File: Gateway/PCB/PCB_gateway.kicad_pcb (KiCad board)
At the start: 2 copper layers, 38 x 52 mm, 39 parts, among them J1 USB4215-03-A_REVA, J2 Conn_01x06_Pin, J3 Conn_01x04_Pin, J4 Conn_01x04_Pin, U1 ESP32-C3-WROOM-02U-N4, U2 BME680, U4 AMS1117-3.3

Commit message: Add files via upload
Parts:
- added R12: 0, Resistor_SMD:R_0805_2012Metric_Pad1.20x1.40mm_HandSolder, F.Cu at (185.1, 109.8)
- added R13: 0, Resistor_SMD:R_0805_2012Metric_Pad1.20x1.40mm_HandSolder, F.Cu at (185.1, 112.1)
- D3: value D_Schottky_Small_Filled -> D_Schottky
- moved R9 2.81 mm to (185.1, 107.4), turned to 180 degrees
- moved U4 0.62 mm to (177.1, 111.6)
- renumbered S2 to BOOT, S1 to EN1, D1 to LED, D2 to POWER
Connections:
- J1 pad A6: D+ -> Net-(J1-DP1)
- J1 pad A7: D- -> Net-(J1-DN1)
- J1 pad B6: D+ -> Net-(J1-DP1)
- J1 pad B7: D- -> Net-(J1-DN1)
- J3 pad 2: RX -> TX
- J3 pad 3: TX -> RX
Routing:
- net Net-(J1-DP1): track 0.00 -> 32.4 mm
- net GPIO3: track 27.9 -> 52.8 mm
- net Net-(J1-DN1): track 0.00 -> 18.3 mm
- net D+: track 41.7 -> 23.9 mm
- net D-: track 38.9 -> 21.2 mm
- net +3.3V: track 156.2 -> 142.0 mm, vias 0 -> 2
- net LED: track 29.3 -> 40.7 mm
- net GND: track 27.0 -> 16.5 mm, vias 26 -> 57
- net SDA: track 33.0 -> 42.5 mm, vias 2 -> 5
- net BOOT: track 41.9 -> 35.4 mm
- net EN: track 60.6 -> 67.1 mm
- net TX: track 8.93 -> 4.40 mm
- net GPIO4: track 27.9 -> 24.2 mm
- net Net-(D3-A): track 9.09 -> 11.4 mm, vias 0 -> 2
- net SCL: track 28.6 -> 30.7 mm
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
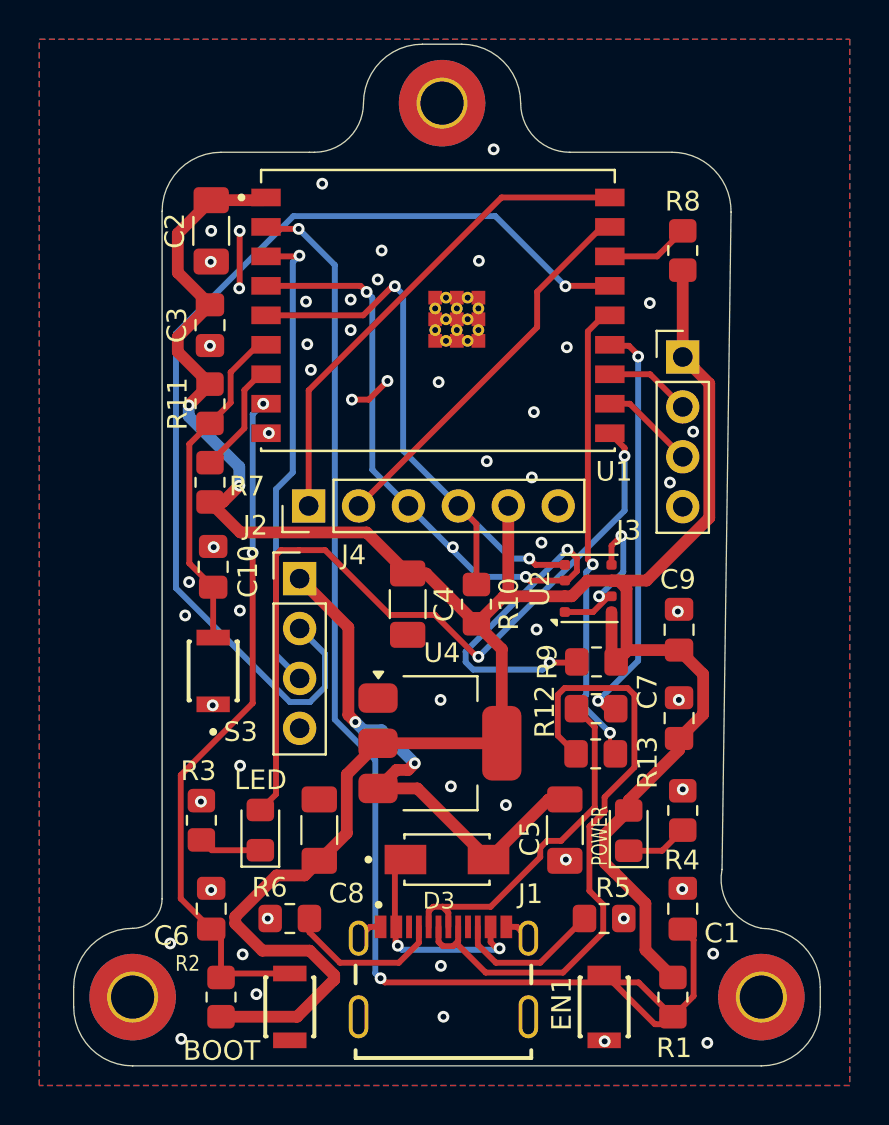
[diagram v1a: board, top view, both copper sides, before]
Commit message: Update PCB design
DRC errors opgelost, teardrops toegevoegd, routing optimaliseren, kleine details
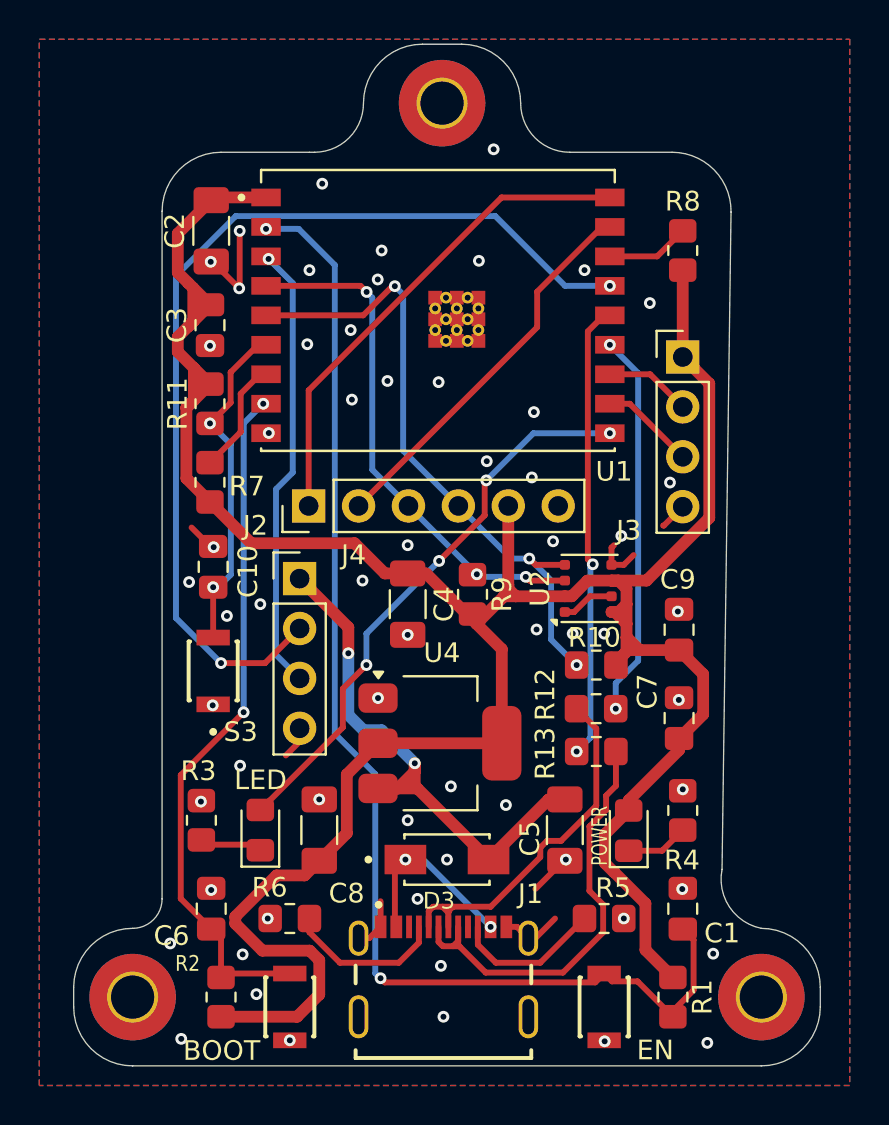
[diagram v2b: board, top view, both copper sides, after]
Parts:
- moved R9 7.19 mm to (178.8, 104.0), turned to 90 degrees
- moved R10 6.84 mm to (185.1, 107.6), turned to 0 degrees
- moved R13 0.12 mm to (185.1, 112.0), turned to 0 degrees
- renumbered EN1 to EN
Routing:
- net SDA: track 42.5 -> 26.6 mm, vias 5 -> 3
- net LED: track 40.7 -> 29.5 mm, vias 2 -> 4
- net Net-(J1-DP1): track 32.4 -> 23.2 mm
- net GND: track 16.5 -> 21.9 mm, vias 57 -> 62
- net EN: track 67.1 -> 63.4 mm
- net +3.3V: track 142.0 -> 145.4 mm, vias 2 -> 0
- net GPIO3: track 52.8 -> 50.2 mm, vias 1 -> 2
- net SCL: track 30.7 -> 32.8 mm, vias 2 -> 3
- net Net-(D3-A): track 11.4 -> 9.43 mm
- net +5V: track 27.0 -> 28.6 mm
- net GPIO4: track 24.2 -> 22.9 mm
- net D-: track 21.2 -> 20.2 mm
- net D+: track 23.9 -> 23.3 mm
- net GPIO7: vias 0 -> 2

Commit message: update silkscreen
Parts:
- removed the G*** at (177.4, 105.5)
- added G***: LOGO, LOGO, B.Cu at (177.4, 99.4)
- added G***: LOGO, LOGO, B.Cu at (176.3, 110.2)
- moved G*** 4.20 mm to (183.0, 107.7)
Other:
- board text added: "if my grandmother had wheels, she would have been a bike"

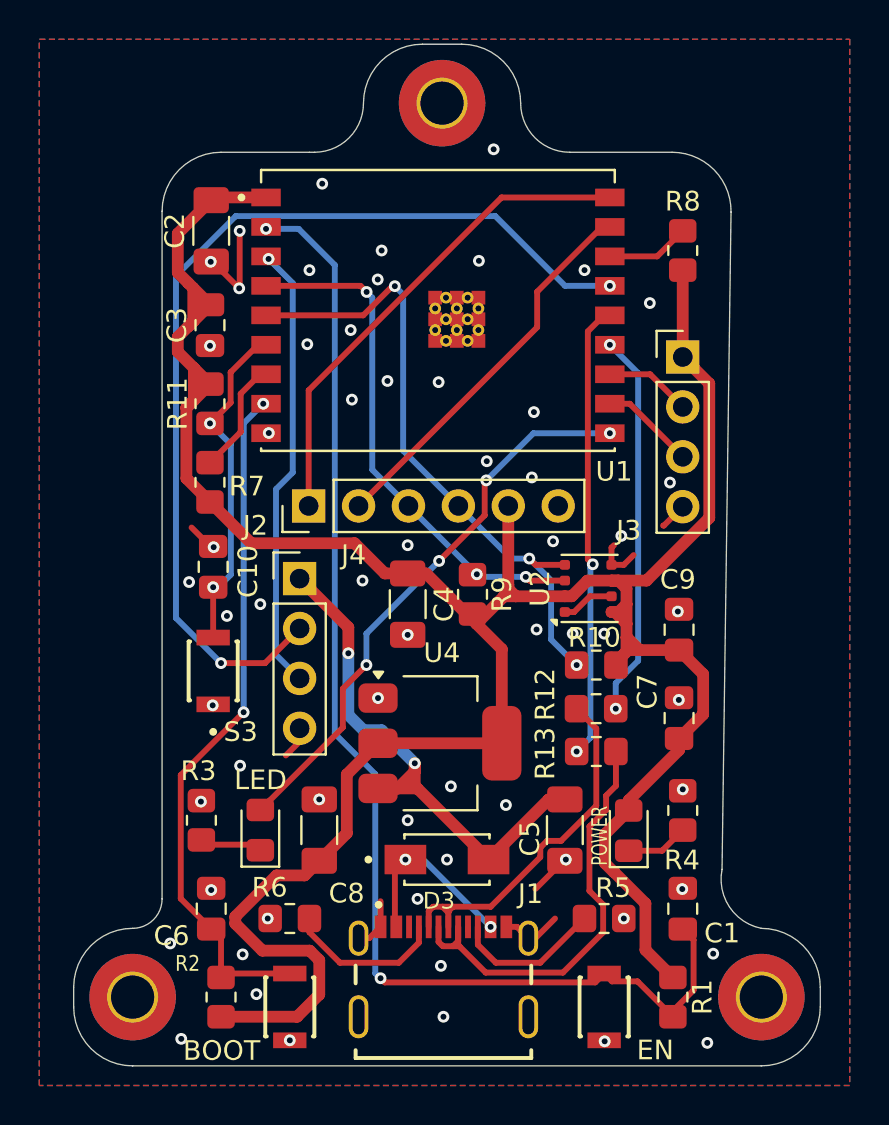
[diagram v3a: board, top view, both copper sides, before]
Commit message: Header silkscreen
added pin description for each header on the silkscreen
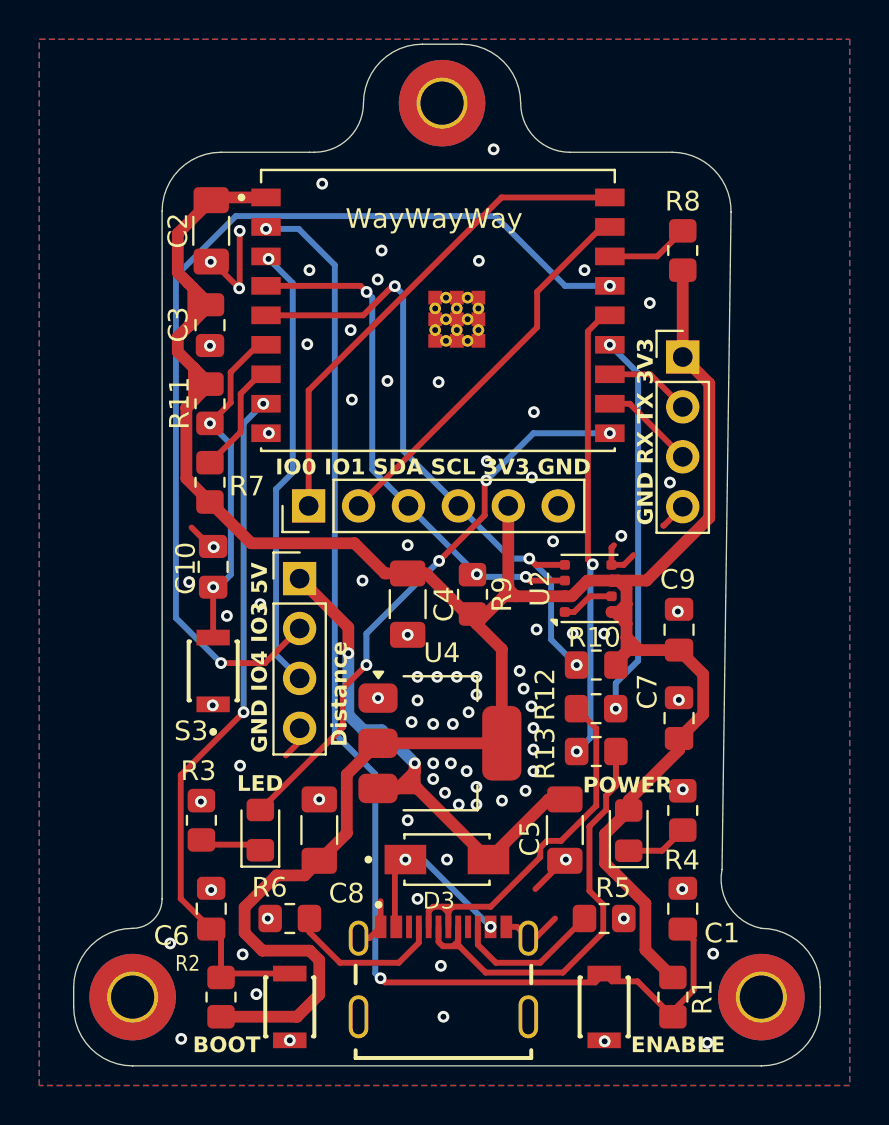
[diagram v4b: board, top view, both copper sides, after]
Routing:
- net GND: vias 62 -> 86
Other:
- board text added: "BOOT"
- board text added: "Distance"
- board text added: "ENABLE"
- board text added: "GND IO4 IO3 5V"
- board text added: "GND RX TX 3V3"
- board text added: "IO0 IO1 SDA SCL 3V3 GND"
- board text added: "LED"
- board text added: "POWER"
- board text added: "WayWayWay"

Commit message: Add files via upload
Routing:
- net +3.3V: track 145.0 -> 143.5 mm
- net GND: track 21.9 -> 21.0 mm
